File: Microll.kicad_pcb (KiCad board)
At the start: 2 copper layers, 35 x 43.2 mm, 30 parts, among them J1 Conn_01x08, J2 Conn_01x08, J3 Conn_01x08, J4 USB_C_Receptacle, J5 Conn_01x08, U1 ESP32-C3-WROOM-02-N4, U2 TLV76733DRVx, U3 STM32G0B1CBU6, U4 USBLC6-2P6, U5 DPDT_Switch_x2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

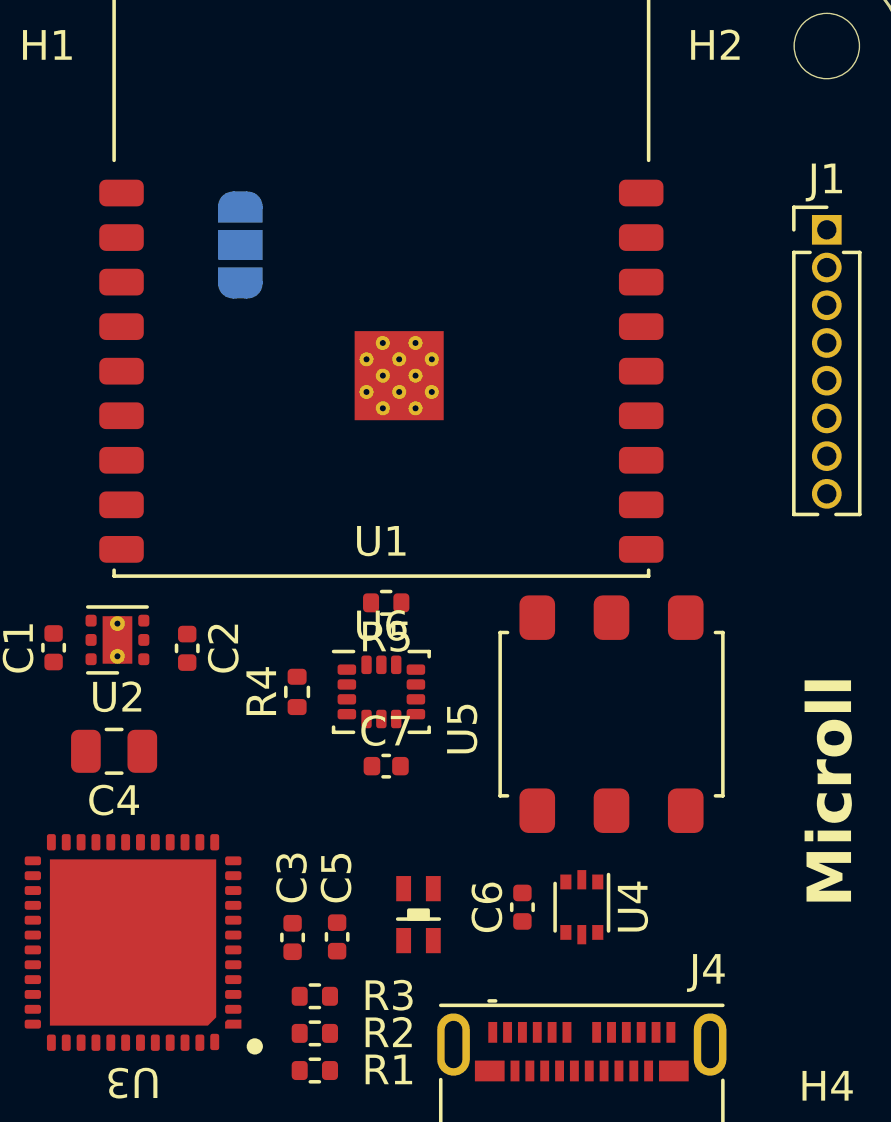
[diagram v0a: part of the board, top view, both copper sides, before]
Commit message: Board ready for track routing
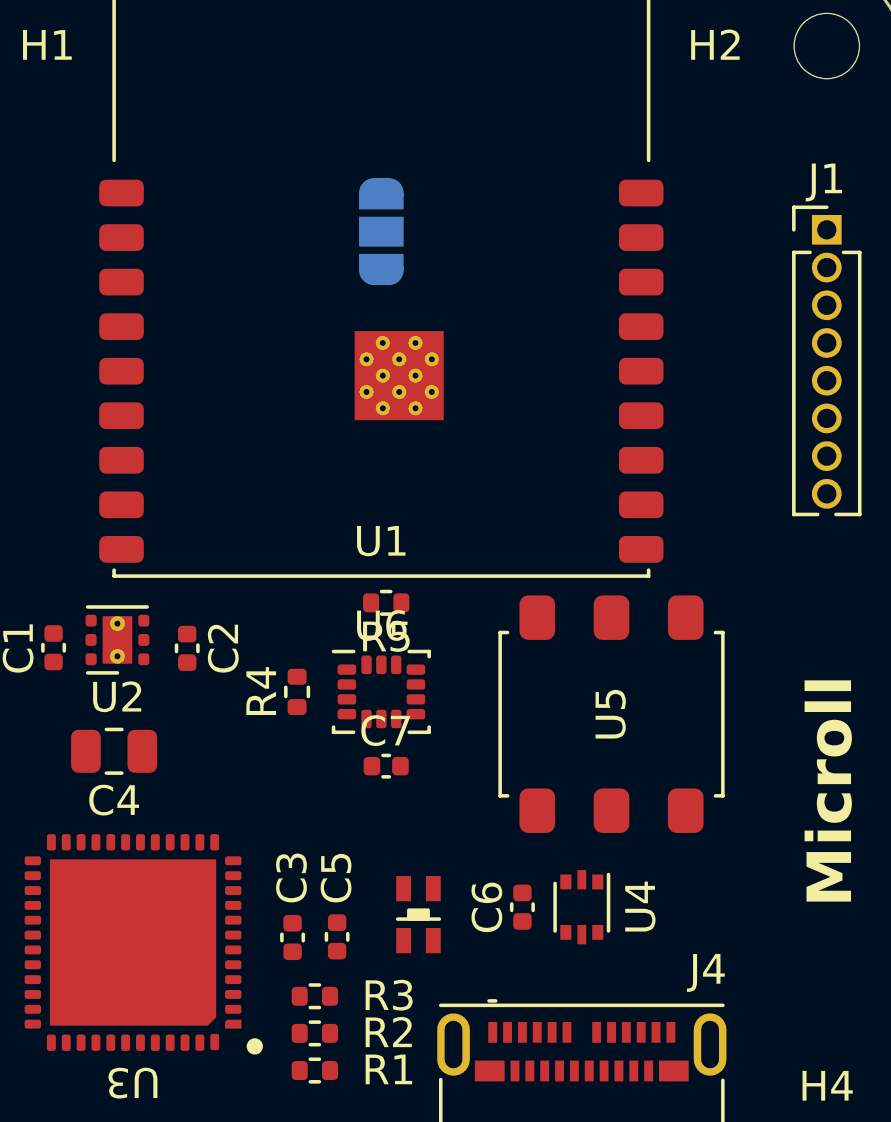
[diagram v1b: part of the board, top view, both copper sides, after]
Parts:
- moved JP1 4.77 mm to (120.0, 101.2)
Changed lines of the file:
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@@
   )
   (setup
+    (stackup
+      (layer "F.SilkS" (type "Top Silk Screen"))
+      (layer "F.Paste" (type "Top Solder Paste"))
+      (layer "F.Mask" (type "Top Solder Mask") (color "Black") (thickness 0.01))
+      (layer "F.Cu" (type "copper") (thickness 0.035))
+      (layer "dielectric 1" (type "core") (thickness 1.51) (material "FR4") (epsilon_r 4.5) (loss_tangent 0.02))
+      (layer "B.Cu" (type "copper") (thickness 0.035))
+      (layer "B.Mask" (type "Bottom Solder Mask") (color "Black") (thickness 0.01))
+      (layer "B.Paste" (type "Bottom Solder Paste"))
+      (layer "B.SilkS" (type "Bottom Silk Screen"))
+      (copper_finish "HAL lead-free")
+      (dielectric_constraints no)
+    )
     (pad_to_mask_clearance 0)
     (pcbplotparams
@@
       )
     )
-    (model "${KICAD6_3DMODEL_DIR}/Connector_USB.3dshapes/USB_C_Receptacle_Molex_105450-0101.wrl"
-      (offset (xyz 0 0 0))
+    (model "C:/Users/Ruben/Downloads/1054500101_stp/1054500101.stp"
+      (offset (xyz 0 0 1.6))
       (scale (xyz 1 1 1))
       (rotate (xyz 0 0 0))
@@
     (property "ki_keywords" "usb ethernet video")
     (attr smd)
-    (fp_text reference "U4" (at 0 -1.75 90) (layer "F.SilkS")
+    (fp_text reference "U4" (at 0 -2 90) (layer "F.SilkS")
         (effects (font (size 1 1) (thickness 0.15)))
     )
@@
     (property "Sheetname" "")
     (attr smd)
-    (fp_text reference "U5" (at 5 -0.5 90 unlocked) (layer "F.SilkS")
+    (fp_text reference "U5" (at 0 0 90 unlocked) (layer "F.SilkS")
         (effects (font (size 1 1) (thickness 0.15)))
     )
@@
   )
   (footprint "Jumper:SolderJumper-3_P1.3mm_Open_RoundedPad1.0x1.5mm_NumberLabels" (layer "B.Cu")
-    (at 115.25 101.7 -90)
+    (at 120 101.25 -90)
     (descr "SMD Solder 3-pad Jumper, 1x1.5mm rounded Pads, 0.3mm gap, open, labeled with numbers")
     (tags "solder jumper open")

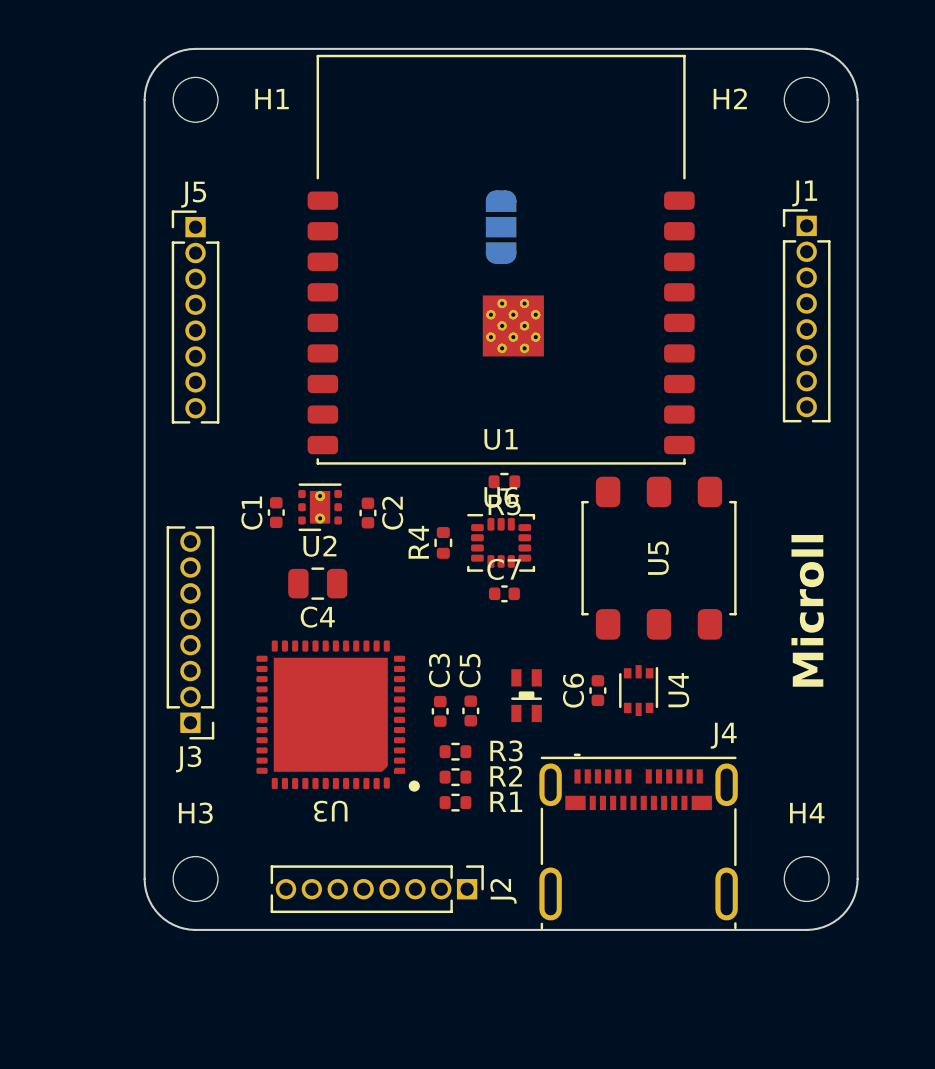
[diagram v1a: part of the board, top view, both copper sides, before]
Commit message: Started routing tracks
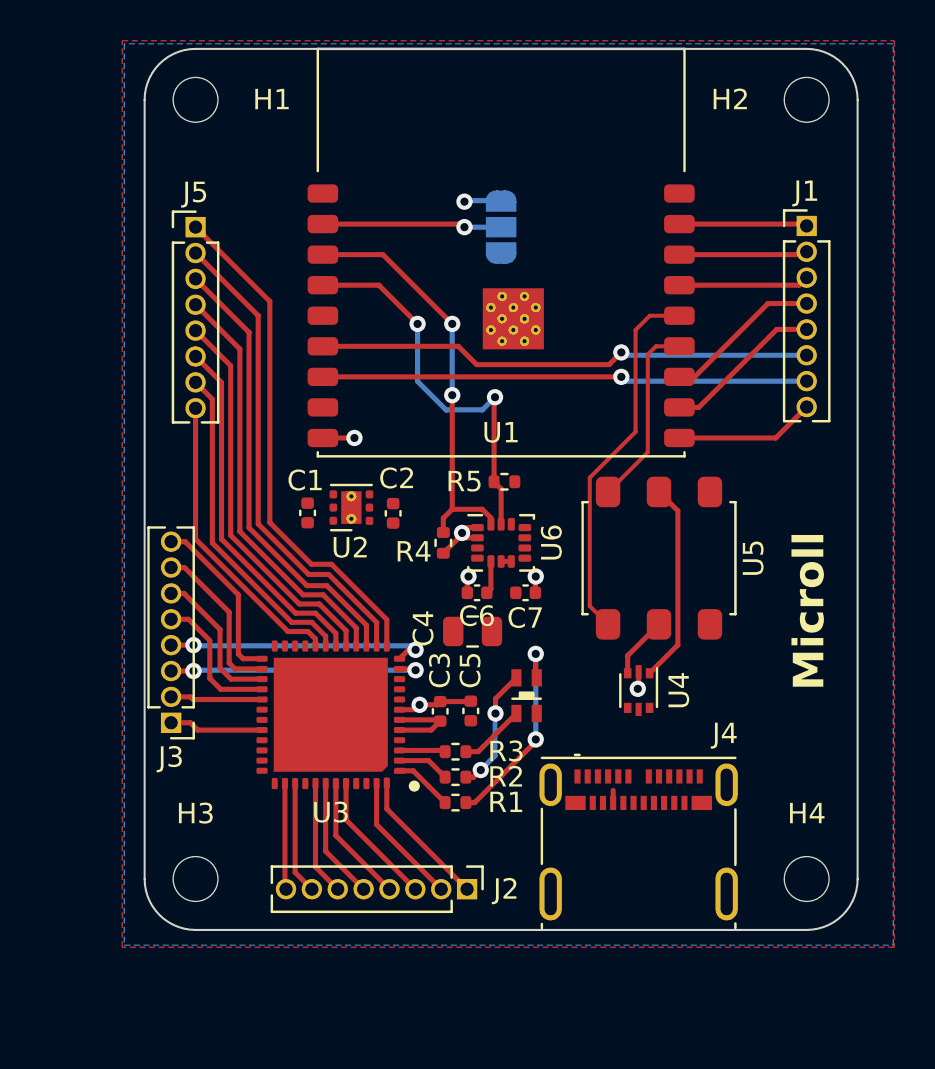
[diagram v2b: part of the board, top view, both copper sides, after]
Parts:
- moved C4 7.96 mm to (118.6, 121.1)
- moved C6 7.63 mm to (118.8, 119.2), turned to 180 degrees
- moved U2 1.54 mm to (112.7, 115.0)
- moved C1 1.54 mm to (110.5, 115.3)
- moved C2 1.24 mm to (114.7, 115.3)
- moved C7 1.04 mm to (121.2, 119.2)
- moved J3 0.95 mm to (103.8, 125.6)
- moved JP2 0.55 mm to (112.3, 125.2), turned to -90 degrees
- moved U1 0.35 mm to (120.0, 105.6)
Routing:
- net SDA: track 0.00 -> 27.4 mm, vias 0 -> 2
- net SCL: track 0.00 -> 25.8 mm, vias 0 -> 2
- net /PA2: track 0.00 -> 25.0 mm
- net /GPIO7: track 0.00 -> 24.4 mm, vias 0 -> 1
- net /GPIO8: track 0.00 -> 23.8 mm, vias 0 -> 1
- net /PA3: track 0.00 -> 23.5 mm
- net /DAC1_OUT1: track 0.00 -> 22.1 mm
- net SPI_SCK: track 0.00 -> 20.6 mm
- net SPI_MISO: track 0.00 -> 19.1 mm
- net ESP32_USB+: track 0.00 -> 18.2 mm
- net SPI_MOSI: track 0.00 -> 17.6 mm
- net /PB0: track 0.00 -> 16.2 mm
- net /PB1: track 0.00 -> 14.7 mm
- net /ADC1_IN1: track 0.00 -> 13.1 mm, vias 0 -> 2
- net /ADC1_IN0: track 0.00 -> 12.8 mm, vias 0 -> 2
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- added copper zone on F.Cu, net +3.3V
- added copper zone on B.Cu, net GND
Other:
- board text added: "ADC1_IN0"
- board text added: "ADC1_IN1"
- board text added: "CAN_RX"
- board text added: "CAN_TX"
- board text added: "DAC1"
- board text added: "GPIO1"
- board text added: "GPIO10"
- board text added: "GPIO2"
- board text added: "GPIO3"
- board text added: "GPIO7"
- board text added: "GPIO8"
- board text added: "MISO"
- board text added: "MOSI"
- board text added: "PA3"
- board text added: "PA8"
- board text added: "PB0"
- board text added: "PB1"
- board text added: "PB13"
- board text added: "PB14"
- board text added: "PB15"
- board text added: "PB3"
- board text added: "PB4"
- board text added: "PB5"
- board text added: "PD3"
- board text added: "Rx"
- board text added: "SCK"
- board text added: "SCL"
- board text added: "SDA"
- board text added: "Tx"
- board text added: "USART_RX"
- board text added: "USART_TX"

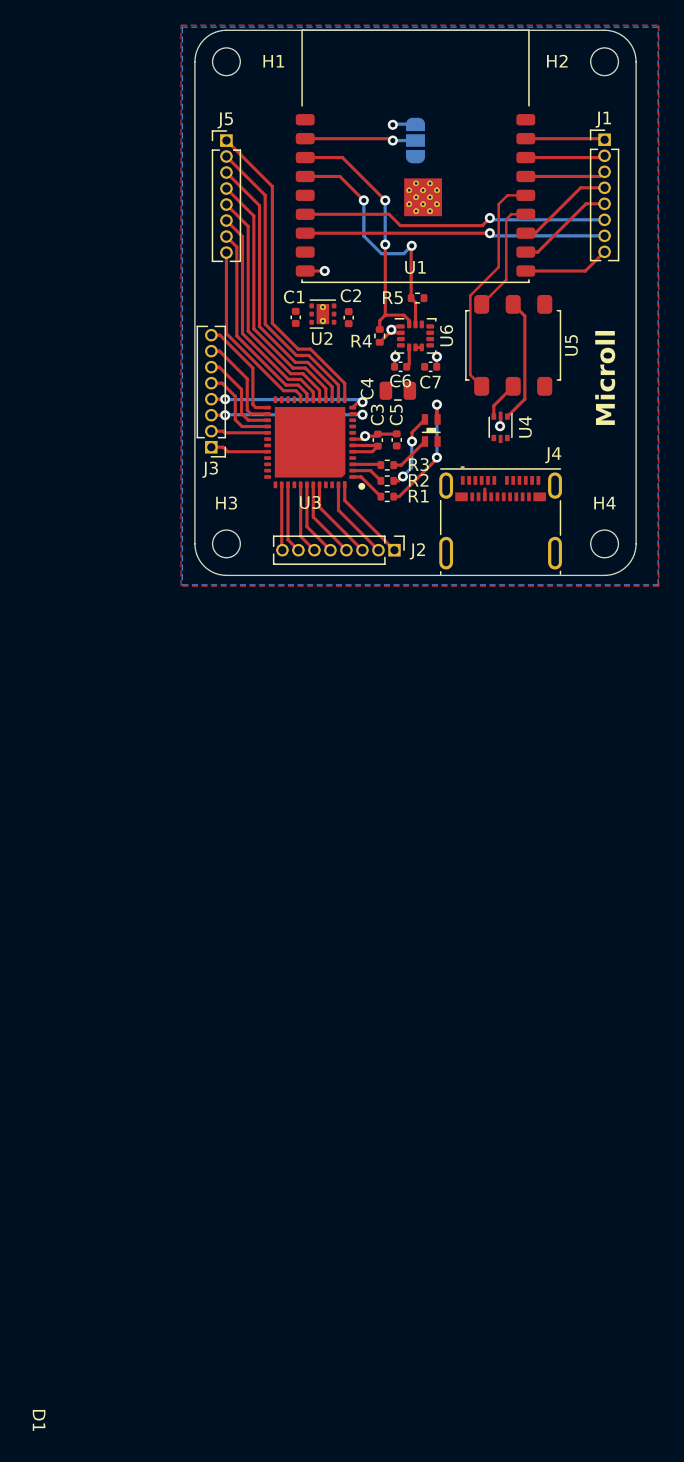
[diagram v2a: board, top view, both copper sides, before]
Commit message: finished routing. Need to clear DRC errors
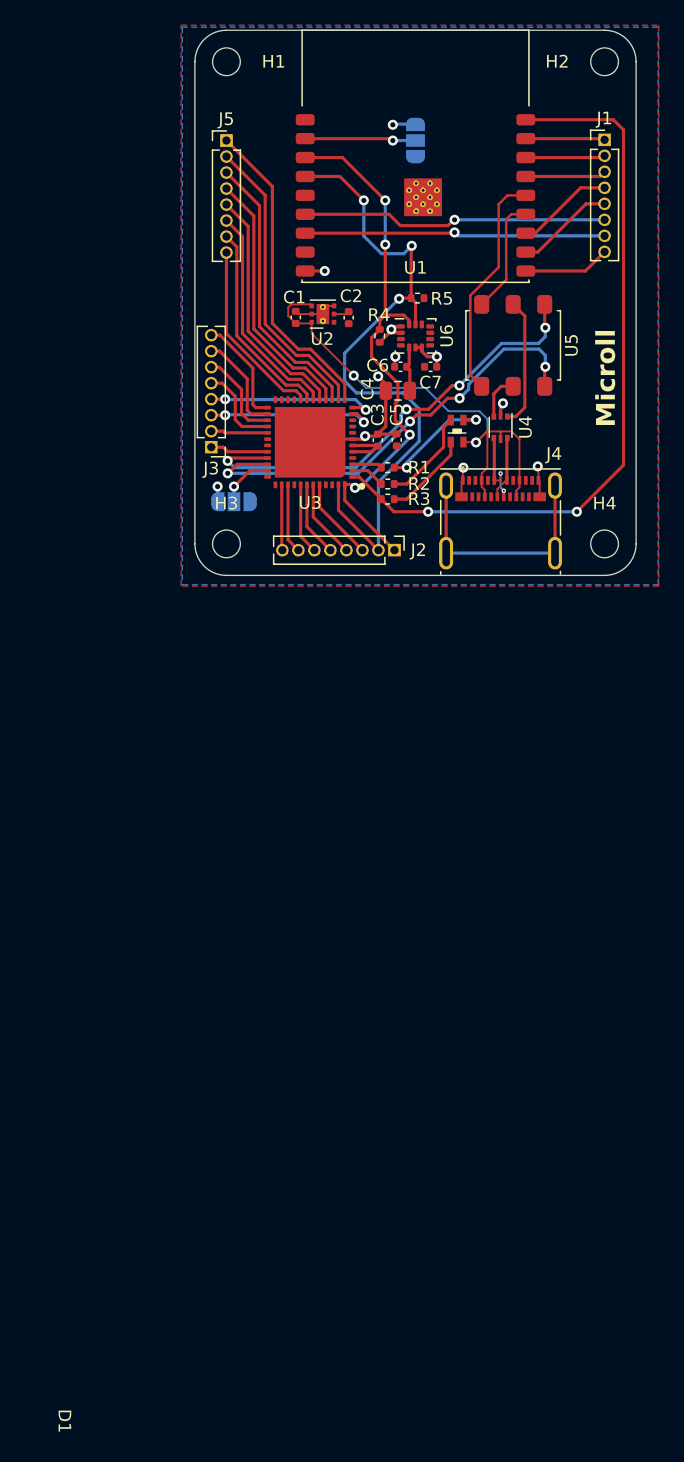
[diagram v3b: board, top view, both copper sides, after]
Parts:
- moved JP2 8.18 mm to (105.6, 129.9), turned to 0 degrees
- moved R3 2.70 mm to (117.8, 129.7)
- moved R1 2.30 mm to (117.8, 127.2)
- moved D1 2.05 mm to (123.3, 124.3)
- moved R2 0.25 mm to (117.8, 128.5)
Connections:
- U3 pad 1: /Red -> /Blue
- U3 pad 3: /Blue -> /Red
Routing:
- net /Blue: track 2.26 -> 58.8 mm, vias 0 -> 2
- net +5V: track 0.61 -> 40.5 mm, vias 0 -> 2
- net STM32_USB-: track 0.00 -> 35.9 mm, vias 0 -> 4
- net STM32_USB+: track 0.00 -> 35.8 mm, vias 0 -> 4
- net SCL: track 25.8 -> 54.5 mm, vias 2 -> 3
- net unconnected-(J4-SHIELD-PadS1): track 0.00 -> 19.4 mm
- net GND: track 8.21 -> 26.7 mm, vias 5 -> 8
- net SDA: track 27.4 -> 44.6 mm, vias 2 -> 4
- net /D+: track 0.00 -> 6.41 mm, vias 0 -> 2
- net /D-: track 0.00 -> 5.08 mm
- net Net-(JP2-C): track 0.00 -> 4.09 mm, vias 0 -> 1
- net Net-(D1-BK): track 3.26 -> 6.96 mm
- net +3.3V: track 10.7 -> 13.7 mm, vias 2 -> 3
- net Net-(D1-GK): track 6.12 -> 7.51 mm, vias 2 -> 0
- net Net-(U2-SNS): track 0.00 -> 1.24 mm
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
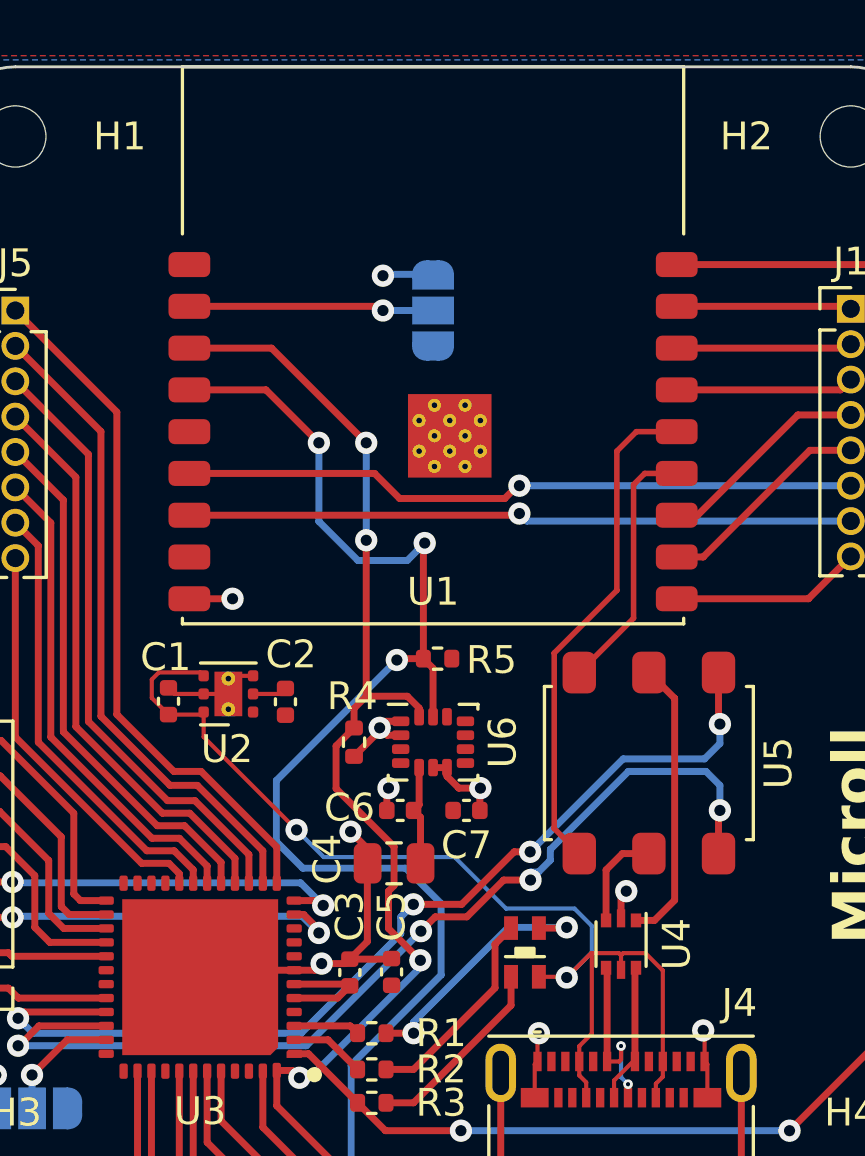
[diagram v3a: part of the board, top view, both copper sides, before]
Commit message: Finishhed Microll PCB
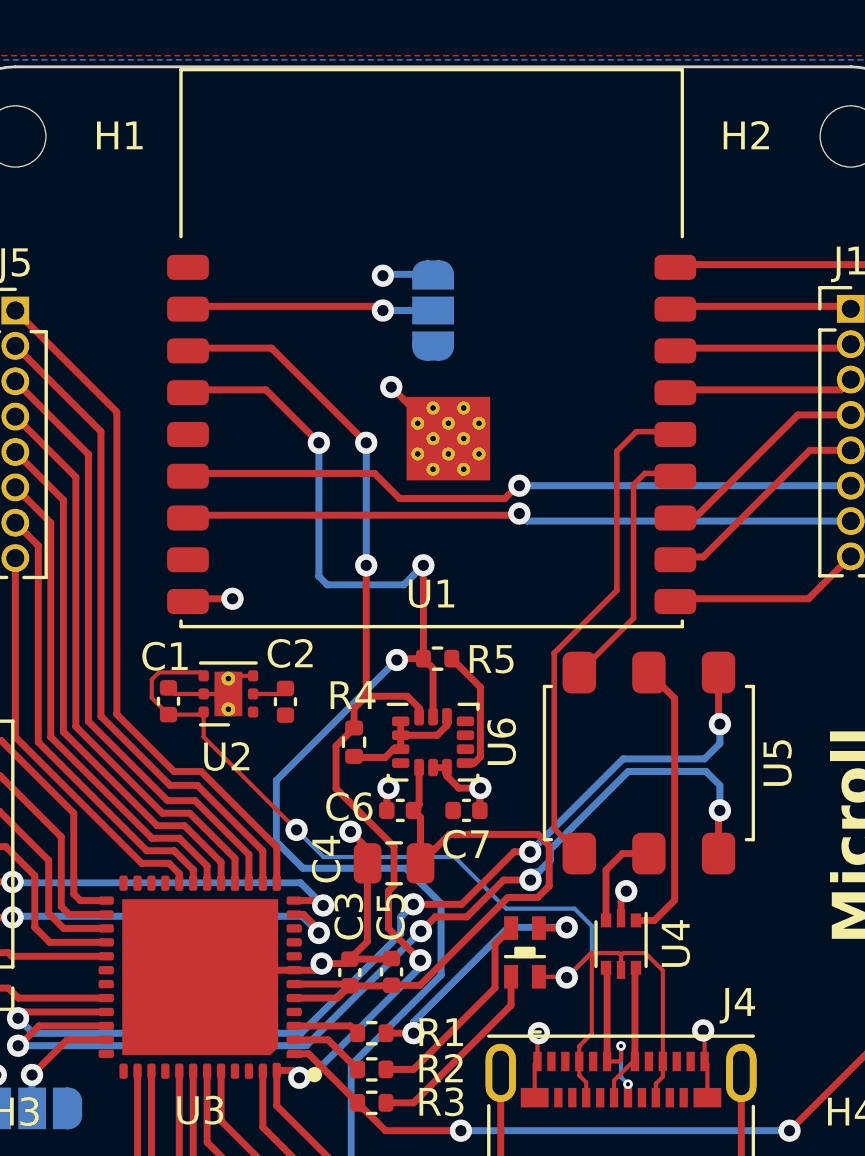
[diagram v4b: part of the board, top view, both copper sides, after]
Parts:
- moved U1 0.11 mm to (120.0, 105.7)
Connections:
- U1 pad TP: unconnected-(U1-PadTP) -> GND
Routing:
- net +3.3V: track 13.7 -> 35.4 mm, vias 3 -> 2
- net GND: track 26.7 -> 30.2 mm, vias 8 -> 9
- net SCL: track 54.5 -> 55.2 mm
